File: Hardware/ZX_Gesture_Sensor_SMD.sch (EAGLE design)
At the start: 50 parts, among them Q1 MMBT2222A, Q2 MOSFET-NCHANNEL2N7002PW, U1 PIC16F1823-14PINTSSOP, U2 MCP6021T-E/OT, U3 DMC2700UDM, U4 DMC2700UDM, U5 TSOP57238TT1

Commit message: V04 changes
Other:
- note added: "v04"
- note removed: "v03"
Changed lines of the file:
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@@
 <text x="172.212" y="11.684" size="1.778" layer="94" font="vector">Shawn Hymel </text>
 <text x="177.8" y="7.62" size="1.778" layer="94">Mary West </text>
-<text x="241.3" y="7.62" size="1.778" layer="94">v03</text>
+<text x="241.3" y="7.62" size="1.778" layer="94">v04</text>
 </plain>
 <instances>
@@
 <pinref part="R9" gate="G$1" pin="1"/>
 <wire x1="223.52" y1="78.74" x2="223.52" y2="76.2" width="0.1524" layer="91"/>
-<wire x1="223.52" y1="76.2" x2="220.98" y2="76.2" width="0.1524" layer="91"/>
-<label x="220.98" y="76.2" size="1.27" layer="95" rot="R180" xref="yes"/>
-</segment>
-</net>
+<wire x1="223.52" y1="76.2" x2="215.9" y2="76.2" width="0.1524" layer="91"/>
+<label x="215.9" y="76.2" size="1.27" layer="95" rot="R180" xref="yes"/>
+</segment>
+</net>

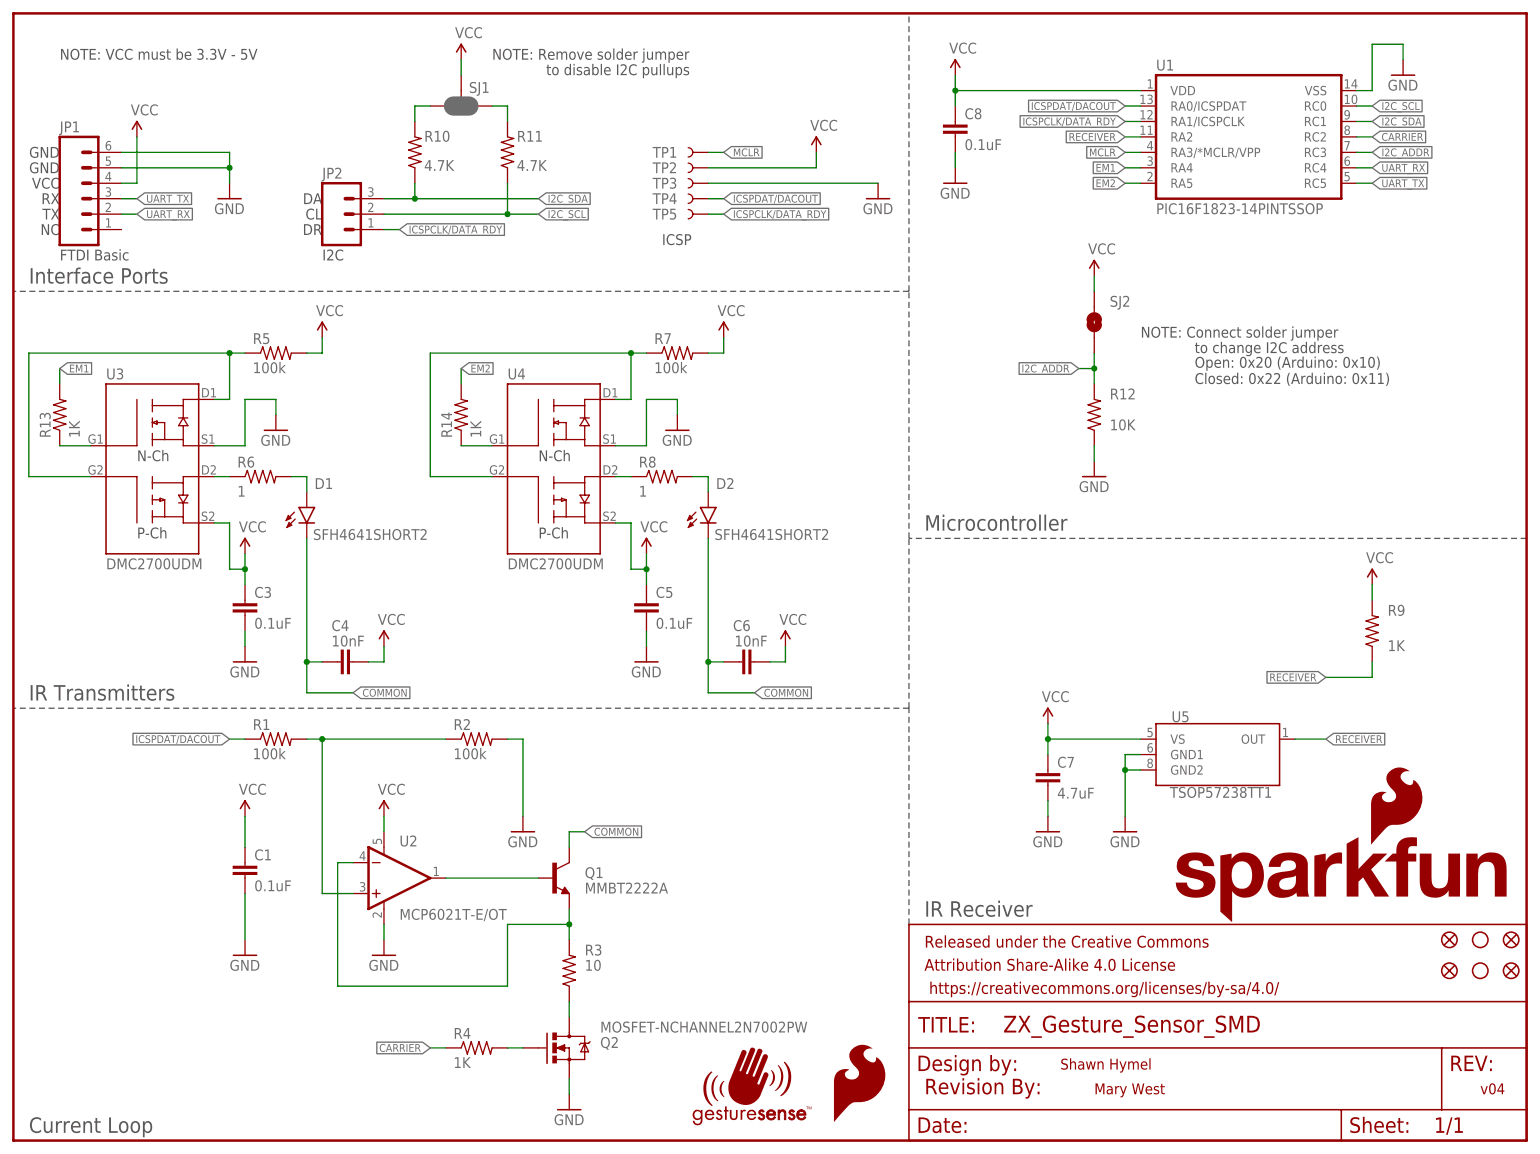
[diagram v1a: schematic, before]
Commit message: Updated Brd File per Engineering Design Review
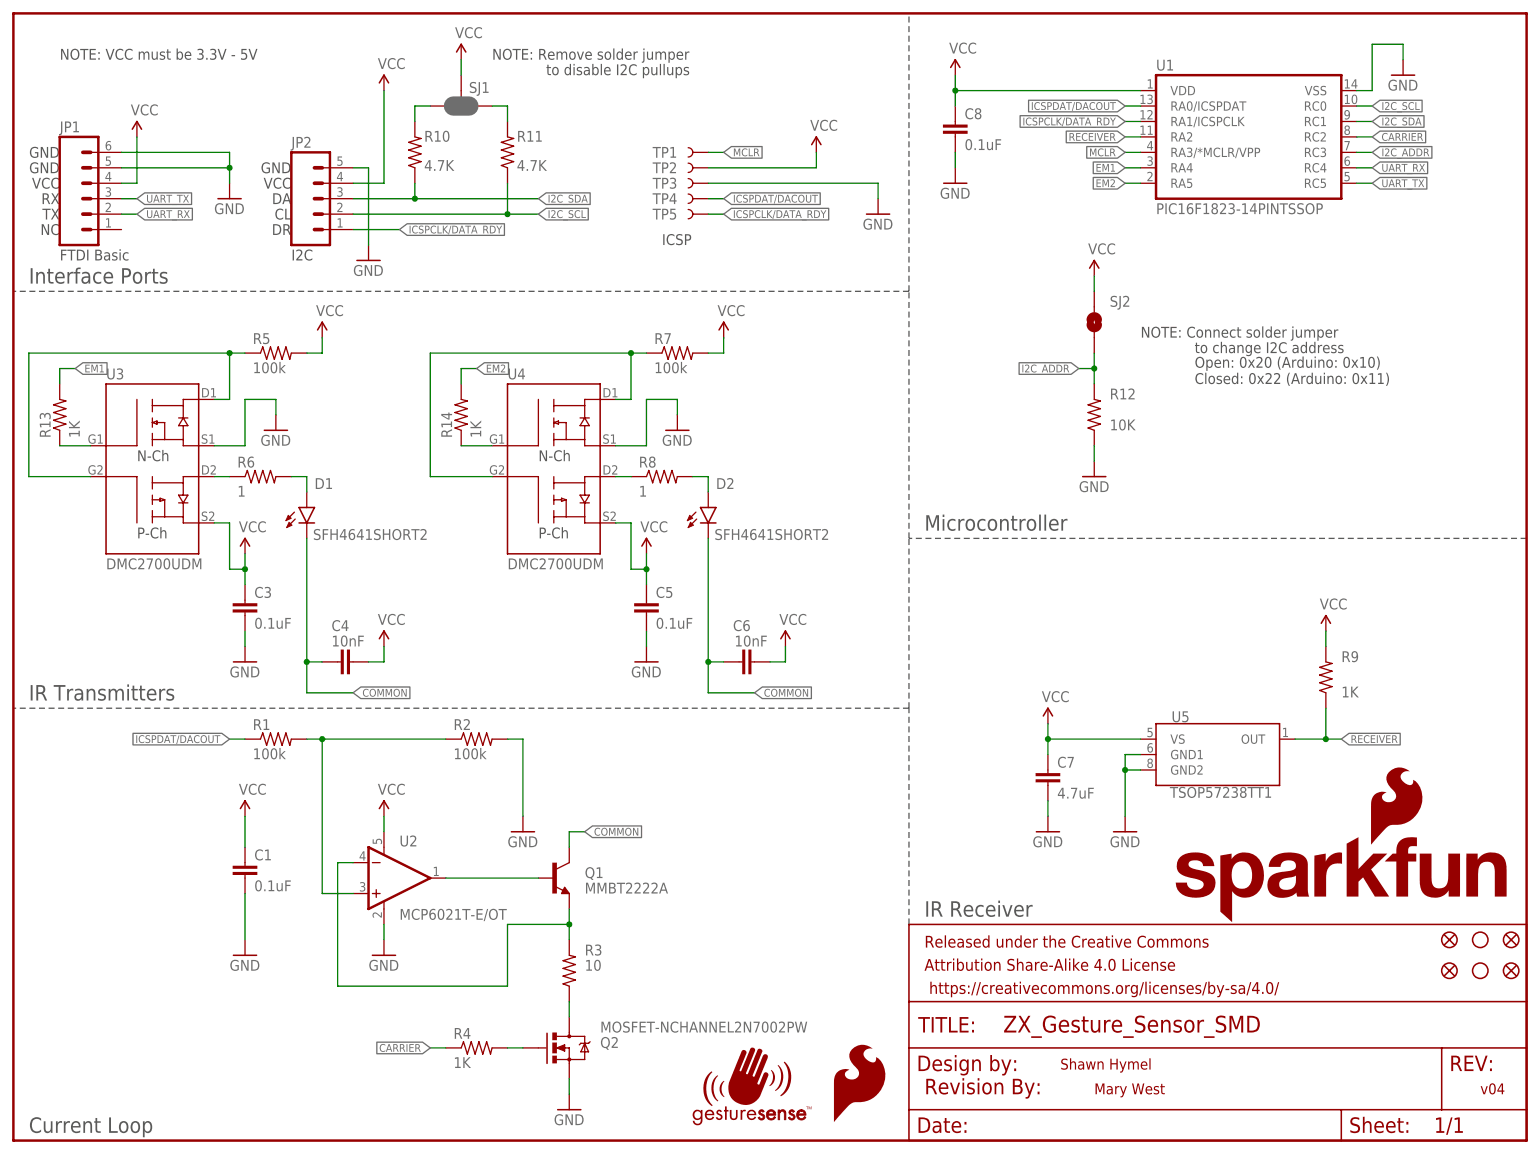
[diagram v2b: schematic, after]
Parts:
- JP2: device SparkFun-Connectors:M031X03_NO_SILK -> SparkFun-Connectors:M05PTH
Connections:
- net GND: now also JP2.5
- net VCC: now also JP2.4
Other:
- moved on the sheet: R9
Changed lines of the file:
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@@
 <layer number="112" name="tSilk" color="7" fill="1" visible="yes" active="yes"/>
 <layer number="113" name="IDFDebug" color="7" fill="1" visible="yes" active="yes"/>
+<layer number="114" name="Badge_Outline" color="7" fill="1" visible="yes" active="yes"/>
+<layer number="115" name="ReferenceISLANDS" color="7" fill="1" visible="yes" active="yes"/>
 <layer number="116" name="Patch_BOT" color="9" fill="4" visible="yes" active="yes"/>
+<layer number="118" name="Rect_Pads" color="7" fill="1" visible="yes" active="yes"/>
 <layer number="121" name="_tsilk" color="7" fill="1" visible="yes" active="yes"/>
 <layer number="122" name="_bsilk" color="7" fill="1" visible="yes" active="yes"/>
@@
 <part name="U5" library="SparkFun-Sensors" deviceset="TSOP57238TT1" device=""/>
 <part name="JP1" library="SparkFun-Connectors" deviceset="M06" device="NO_SILK_FEMALE_PTH"/>
-<part name="JP2" library="SparkFun-Connectors" deviceset="M03" device="1X03_NO_SILK"/>
+<part name="JP2" library="SparkFun-Connectors" deviceset="M05" device="PTH"/>
 <part name="GND1" library="SparkFun-Aesthetics" deviceset="GND" device=""/>
 <part name="SUPPLY1" library="SparkFun-Aesthetics" deviceset="VCC" device=""/>
@@
 <part name="LOGO2" library="SparkFun-Aesthetics" deviceset="SFE_LOGO_FLAME" device=".1_INCH" value="SFE_LOGO_FLAME.1_INCH"/>
 <part name="FID3" library="SparkFun-Aesthetics" deviceset="FIDUCIAL" device="UFIDUCIAL" value="FIDUCIALUFIDUCIAL"/>
+<part name="GND16" library="SparkFun-Aesthetics" deviceset="GND" device=""/>
+<part name="SUPPLY16" library="SparkFun-Aesthetics" deviceset="VCC" device=""/>
 </parts>
 <sheets>
@@
 <plain>
 <text x="7.62" y="144.78" size="1.778" layer="97" font="vector">FTDI Basic</text>
-<text x="50.8" y="144.78" size="1.778" layer="97">I2C</text>
+<text x="45.72" y="144.78" size="1.778" layer="97">I2C</text>
 <text x="106.68" y="147.32" size="1.778" layer="97" font="vector">ICSP</text>
 <wire x1="147.32" y1="35.56" x2="147.32" y2="71.12" width="0.1524" layer="97" style="longdash"/>
@@
 <text x="7.62" y="160.02" size="1.778" layer="97" align="center-right">GND</text>
 <text x="7.62" y="162.56" size="1.778" layer="97" align="center-right">GND</text>
-<text x="50.8" y="154.94" size="1.778" layer="97" align="center-right">DA</text>
-<text x="50.8" y="152.4" size="1.778" layer="97" align="center-right">CL</text>
-<text x="50.8" y="149.86" size="1.778" layer="97" align="center-right">DR</text>
+<text x="45.72" y="154.94" size="1.778" layer="97" align="center-right">DA</text>
+<text x="45.72" y="152.4" size="1.778" layer="97" align="center-right">CL</text>
+<text x="45.72" y="149.86" size="1.778" layer="97" align="center-right">DR</text>
 <text x="7.62" y="149.86" size="1.778" layer="97" align="center-right">NC</text>
 <text x="7.62" y="177.8" size="1.778" layer="97" font="vector">NOTE: VCC must be 3.3V - 5V</text>
@@
 <text x="177.8" y="7.62" size="1.778" layer="94">Mary West </text>
 <text x="241.3" y="7.62" size="1.778" layer="94">v04</text>
+<text x="45.72" y="160.02" size="1.778" layer="97" align="center-right">GND</text>
+<text x="45.72" y="157.48" size="1.778" layer="97" align="center-right">VCC</text>
 </plain>
 <instances>
@@
 <attribute name="NAME" x="7.62" y="165.862" size="1.778" layer="95"/>
 </instance>
-<instance part="JP2" gate="G$1" x="53.34" y="152.4"/>
+<instance part="JP2" gate="G$1" x="48.26" y="154.94"/>
 <instance part="GND1" gate="1" x="35.56" y="154.94"/>
 <instance part="SUPPLY1" gate="G$1" x="20.32" y="165.1"/>
 <instance part="SUPPLY2" gate="G$1" x="132.08" y="162.56"/>
-<instance part="GND2" gate="1" x="142.24" y="154.94"/>
+<instance part="GND2" gate="1" x="142.24" y="152.4"/>
 <instance part="R1" gate="G$1" x="43.18" y="66.04"/>
 <instance part="R2" gate="G$1" x="76.2" y="66.04"/>
@@
 <instance part="SUPPLY10" gate="G$1" x="104.14" y="96.52"/>
 <instance part="GND10" gate="1" x="104.14" y="78.74"/>
-<instance part="R9" gate="G$1" x="223.52" y="83.82" smashed="yes" rot="R90">
-<attribute name="NAME" x="226.06" y="86.3346" size="1.778" layer="95"/>
-<attribute name="VALUE" x="226.06" y="80.518" size="1.778" layer="96"/>
+<instance part="R9" gate="G$1" x="215.9" y="76.2" smashed="yes" rot="R90">
+<attribute name="NAME" x="218.44" y="78.7146" size="1.778" layer="95"/>
+<attribute name="VALUE" x="218.44" y="72.898" size="1.778" layer="96"/>
 </instance>
 <instance part="C7" gate="G$1" x="170.18" y="58.42"/>
 <instance part="GND11" gate="1" x="182.88" y="50.8"/>
 <instance part="SUPPLY11" gate="G$1" x="170.18" y="68.58"/>
-<instance part="SUPPLY12" gate="G$1" x="223.52" y="91.44"/>
+<instance part="SUPPLY12" gate="G$1" x="215.9" y="83.82"/>
 <instance part="GND12" gate="1" x="170.18" y="50.8"/>
 <instance part="GND13" gate="1" x="228.6" y="175.26"/>
@@
 <instance part="LOGO2" gate="G$1" x="134.62" y="2.54"/>
 <instance part="FID3" gate="G$1" x="236.22" y="27.94"/>
+<instance part="GND16" gate="1" x="58.42" y="144.78"/>
+<instance part="SUPPLY16" gate="G$1" x="60.96" y="172.72"/>
 </instances>
 <busses>
@@
 <pinref part="SUPPLY12" gate="G$1" pin="VCC"/>
 <pinref part="R9" gate="G$1" pin="2"/>
-<wire x1="223.52" y1="91.44" x2="223.52" y2="88.9" width="0.1524" layer="91"/>
+<wire x1="215.9" y1="83.82" x2="215.9" y2="81.28" width="0.1524" layer="91"/>
 </segment>
 <segment>
@@
 <wire x1="124.46" y1="78.74" x2="127" y2="78.74" width="0.1524" layer="91"/>
 <wire x1="127" y1="78.74" x2="127" y2="81.28" width="0.1524" layer="91"/>
+</segment>
+<segment>
+<pinref part="JP2" gate="G$1" pin="4"/>
+<wire x1="55.88" y1="157.48" x2="60.96" y2="157.48" width="0.1524" layer="91"/>
+<wire x1="60.96" y1="157.48" x2="60.96" y2="172.72" width="0.1524" layer="91"/>
+<pinref part="SUPPLY16" gate="G$1" pin="VCC"/>
 </segment>
 </net>
@@
 </segment>
 <segment>
-<pinref part="GND2" gate="1" pin="GND"/>
-<wire x1="114.3" y1="157.48" x2="142.24" y2="157.48" width="0.1524" layer="91"/>
-<pinref part="TP3" gate="G$1" pin="1"/>
-</segment>
-<segment>
 <pinref part="R2" gate="G$1" pin="2"/>
 <wire x1="81.28" y1="66.04" x2="83.82" y2="66.04" width="0.1524" layer="91"/>
@@
 <wire x1="177.8" y1="111.76" x2="177.8" y2="114.3" width="0.1524" layer="91"/>
 </segment>
+<segment>
+<pinref part="JP2" gate="G$1" pin="5"/>
+<wire x1="55.88" y1="160.02" x2="58.42" y2="160.02" width="0.1524" layer="91"/>
+<wire x1="58.42" y1="160.02" x2="58.42" y2="147.32" width="0.1524" layer="91"/>
+<pinref part="GND16" gate="1" pin="GND"/>
+</segment>
+<segment>
+<pinref part="GND2" gate="1" pin="GND"/>
+<wire x1="142.24" y1="154.94" x2="142.24" y2="157.48" width="0.1524" layer="91"/>
+<pinref part="TP3" gate="G$1" pin="1"/>
+<wire x1="142.24" y1="157.48" x2="114.3" y2="157.48" width="0.1524" layer="91"/>
+</segment>
 </net>
 <net name="I2C_SDA" class="0">
 <segment>
 <pinref part="JP2" gate="G$1" pin="3"/>
-<wire x1="60.96" y1="154.94" x2="66.04" y2="154.94" width="0.1524" layer="91"/>
+<wire x1="55.88" y1="154.94" x2="66.04" y2="154.94" width="0.1524" layer="91"/>
 <label x="86.36" y="154.94" size="1.27" layer="95" xref="yes"/>
 <pinref part="R10" gate="G$1" pin="1"/>
@@
 <segment>
 <pinref part="JP2" gate="G$1" pin="2"/>
-<wire x1="60.96" y1="152.4" x2="81.28" y2="152.4" width="0.1524" layer="91"/>
+<wire x1="55.88" y1="152.4" x2="81.28" y2="152.4" width="0.1524" layer="91"/>
 <label x="86.36" y="152.4" size="1.27" layer="95" xref="yes"/>
 <pinref part="R11" gate="G$1" pin="1"/>
@@
 <segment>
 <pinref part="JP2" gate="G$1" pin="1"/>
-<wire x1="60.96" y1="149.86" x2="63.5" y2="149.86" width="0.1524" layer="91"/>
+<wire x1="55.88" y1="149.86" x2="63.5" y2="149.86" width="0.1524" layer="91"/>
 <label x="63.5" y="149.86" size="1.27" layer="95" xref="yes"/>
 </segment>
@@
 <segment>
 <pinref part="R13" gate="G$1" pin="2"/>
-<wire x1="7.62" y1="124.46" x2="7.62" y2="127" width="0.1524" layer="91"/>
-<label x="7.62" y="127" size="1.27" layer="95" xref="yes"/>
+<label x="10.16" y="127" size="1.27" layer="95" xref="yes"/>
+<wire x1="10.16" y1="127" x2="7.62" y2="127" width="0.1524" layer="91"/>
+<wire x1="7.62" y1="127" x2="7.62" y2="124.46" width="0.1524" layer="91"/>
 </segment>
 </net>
@@
 <segment>
 <pinref part="R14" gate="G$1" pin="2"/>
-<wire x1="73.66" y1="124.46" x2="73.66" y2="127" width="0.1524" layer="91"/>
-<label x="73.66" y="127" size="1.27" layer="95" xref="yes"/>
+<label x="76.2" y="127" size="1.27" layer="95" xref="yes"/>
+<wire x1="76.2" y1="127" x2="73.66" y2="127" width="0.1524" layer="91"/>
+<wire x1="73.66" y1="127" x2="73.66" y2="124.46" width="0.1524" layer="91"/>
 </segment>
 </net>
@@
 <net name="RECEIVER" class="0">
 <segment>
-<pinref part="U5" gate="G$1" pin="OUT"/>
-<wire x1="210.82" y1="66.04" x2="215.9" y2="66.04" width="0.1524" layer="91"/>
-<label x="215.9" y="66.04" size="1.27" layer="95" xref="yes"/>
-</segment>
-<segment>
 <pinref part="U1" gate="G$1" pin="RA2"/>
 <wire x1="185.42" y1="165.1" x2="182.88" y2="165.1" width="0.1524" layer="91"/>
@@
 <segment>
 <pinref part="R9" gate="G$1" pin="1"/>
-<wire x1="223.52" y1="78.74" x2="223.52" y2="76.2" width="0.1524" layer="91"/>
-<wire x1="223.52" y1="76.2" x2="215.9" y2="76.2" width="0.1524" layer="91"/>
-<label x="215.9" y="76.2" size="1.27" layer="95" rot="R180" xref="yes"/>
-</segment>
-</net>
+<pinref part="U5" gate="G$1" pin="OUT"/>
+<wire x1="210.82" y1="66.04" x2="215.9" y2="66.04" width="0.1524" layer="91"/>
+<label x="218.44" y="66.04" size="1.27" layer="95" xref="yes"/>
+<wire x1="215.9" y1="66.04" x2="218.44" y2="66.04" width="0.1524" layer="91"/>
+<wire x1="215.9" y1="71.12" x2="215.9" y2="66.04" width="0.1524" layer="91"/>
+<junction x="215.9" y="66.04"/>
+</segment>
+</net>

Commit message: Updated SCH & BRD Files
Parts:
- R3: value 10 -> 1K 1%; device SparkFun-Resistors:10OHM-1/10W-5%0603SMD -> SparkFun-Resistors:1KOHM-1/10W-1%(0603)
- U5: value TSOP57238TT1 -> TSSP57038; device SparkFun-Sensors:TSOP57238TT1 -> SparkFun-Sensors:TSSP57038
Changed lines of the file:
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@@
 <?xml version="1.0" encoding="utf-8"?>
 <!DOCTYPE eagle SYSTEM "eagle.dtd">
-<eagle version="7.5.0">
+<eagle version="7.7.0">
 <drawing>
 <settings>
@@
 <part name="U3" library="SparkFun-DiscreteSemi" deviceset="DMC2700UDM" device=""/>
 <part name="U4" library="SparkFun-DiscreteSemi" deviceset="DMC2700UDM" device=""/>
-<part name="U5" library="SparkFun-Sensors" deviceset="TSOP57238TT1" device=""/>
+<part name="U5" library="SparkFun-Sensors" deviceset="TSSP57038" device=""/>
 <part name="JP1" library="SparkFun-Connectors" deviceset="M06" device="NO_SILK_FEMALE_PTH"/>
 <part name="JP2" library="SparkFun-Connectors" deviceset="M05" device="PTH"/>
@@
 <part name="R1" library="SparkFun-Resistors" deviceset="100KOHM-1/10W-1%(0603)" device="" value="100k"/>
 <part name="R2" library="SparkFun-Resistors" deviceset="100KOHM-1/10W-1%(0603)" device="" value="100k"/>
-<part name="R3" library="SparkFun-Resistors" deviceset="10OHM-1/10W-5%0603" device="SMD" value="10"/>
+<part name="R3" library="SparkFun-Resistors" deviceset="1KOHM-1/10W-1%(0603)" device="" value="1K 1%"/>
 <part name="R4" library="SparkFun-Resistors" deviceset="1KOHM-1/10W-1%(0603)" device="" value="1K"/>
 <part name="C1" library="SparkFun-Capacitors" deviceset="0.1UF-25V(+80/-20%)(0603)" device="" value="0.1uF"/>

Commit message: Updated BRD and SCH files
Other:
- note added: "v05"
- note removed: "v04"
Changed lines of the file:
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@@
 <text x="172.212" y="11.684" size="1.778" layer="94" font="vector">Shawn Hymel </text>
 <text x="177.8" y="7.62" size="1.778" layer="94">Mary West </text>
-<text x="241.3" y="7.62" size="1.778" layer="94">v04</text>
+<text x="241.3" y="7.62" size="1.778" layer="94">v05</text>
 <text x="45.72" y="160.02" size="1.778" layer="97" align="center-right">GND</text>
 <text x="45.72" y="157.48" size="1.778" layer="97" align="center-right">VCC</text>

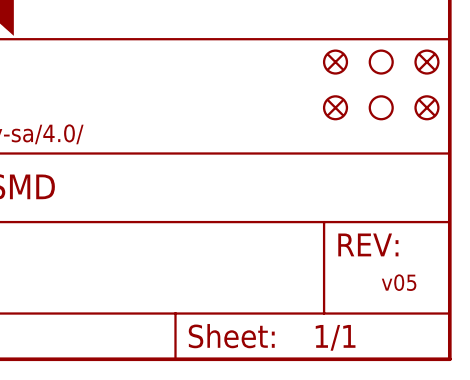
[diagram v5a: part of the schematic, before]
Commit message: -Updated v05 to v10 -moved back silk labels -all copper is unchanged from v05.
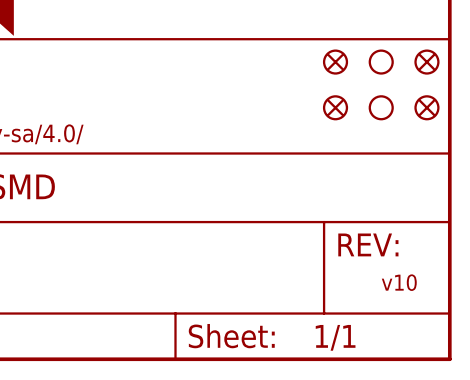
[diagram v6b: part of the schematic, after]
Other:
- note added: "v10"
- note removed: "v05"
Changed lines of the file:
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@@
 <text x="172.212" y="11.684" size="1.778" layer="94" font="vector">Shawn Hymel </text>
 <text x="177.8" y="7.62" size="1.778" layer="94">Mary West </text>
-<text x="241.3" y="7.62" size="1.778" layer="94">v05</text>
+<text x="241.3" y="7.62" size="1.778" layer="94">v10</text>
 <text x="45.72" y="160.02" size="1.778" layer="97" align="center-right">GND</text>
 <text x="45.72" y="157.48" size="1.778" layer="97" align="center-right">VCC</text>
